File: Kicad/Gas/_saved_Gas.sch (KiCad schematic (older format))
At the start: 13 parts, among them J1 MG811, J2 CONN_01X04, J3 MQ135, J4 CCS811, J5 CONN_01X04

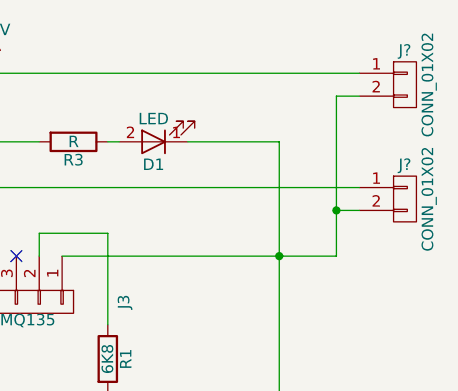
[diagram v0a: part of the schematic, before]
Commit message: Corrected kicad libraries. Added ecoPlanos libs.
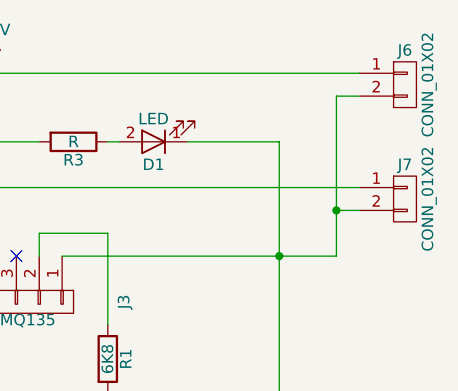
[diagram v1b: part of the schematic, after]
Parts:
- gave numbers to parts that had none: 2
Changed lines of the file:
@@
 EESchema Schematic File Version 2
 LIBS:Gas-rescue
-LIBS:freetronics_schematic
 LIBS:power
 LIBS:device
@@
 LIBS:contrib
 LIBS:valves
-LIBS:mq135
+LIBS:Common-Parts-Library
+LIBS:freetronics_schematic
 LIBS:Gas-cache
 EELAYER 25 0
@@
 $EndDescr
 $Comp
-L GND #PWR3
+L GND #PWR2
 U 1 1 5966646F
 P 4050 3450
-F 0 "#PWR3" H 4050 3200 50  0001 C CNN
+F 0 "#PWR2" H 4050 3200 50  0001 C CNN
 F 1 "GND" H 4050 3300 50  0000 C CNN
 F 2 "" H 4050 3450 50  0001 C CNN
@@
 $EndComp
 $Comp
-L +5V #PWR1
+L +5V #PWR3
 U 1 1 59666483
 P 4250 750
-F 0 "#PWR1" H 4250 600 50  0001 C CNN
+F 0 "#PWR3" H 4250 600 50  0001 C CNN
 F 1 "+5V" H 4250 890 50  0000 C CNN
 F 2 "" H 4250 750 50  0001 C CNN
@@
 $EndComp
 $Comp
-L +3V3 #PWR2
+L +3V3 #PWR1
 U 1 1 59666497
 P 3750 750
-F 0 "#PWR2" H 3750 600 50  0001 C CNN
+F 0 "#PWR1" H 3750 600 50  0001 C CNN
 F 1 "+3V3" H 3750 890 50  0000 C CNN
 F 2 "" H 3750 750 50  0001 C CNN
@@
 	3650 1600 3650 1500
 $Comp
-L CONN_01X02 J?
+L CONN_01X02 J6
 U 1 1 599D8F77
 P 6050 850
-F 0 "J?" H 6050 1000 50  0000 C CNN
+F 0 "J6" H 6050 1000 50  0000 C CNN
 F 1 "CONN_01X02" V 6150 850 50  0000 C CNN
 F 2 "" H 6050 850 50  0001 C CNN
@@
 $EndComp
 $Comp
-L CONN_01X02 J?
+L CONN_01X02 J7
 U 1 1 599D9054
 P 6050 1350
-F 0 "J?" H 6050 1500 50  0000 C CNN
+F 0 "J7" H 6050 1500 50  0000 C CNN
 F 1 "CONN_01X02" V 6150 1350 50  0000 C CNN
 F 2 "" H 6050 1350 50  0001 C CNN
